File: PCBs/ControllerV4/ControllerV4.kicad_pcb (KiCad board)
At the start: 2 copper layers, 116.5 x 53 mm, 7 parts, among them J1 DB25, J2 DB25, T1 TEENSY20

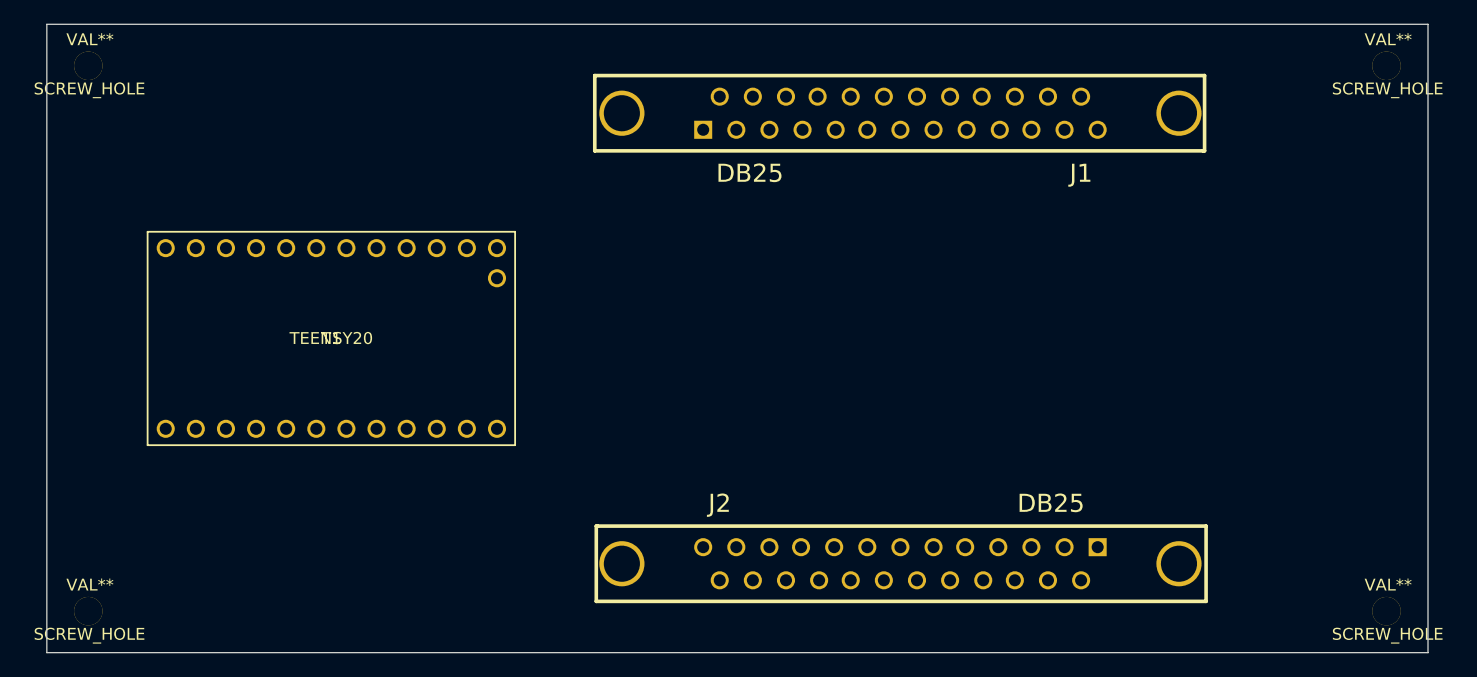
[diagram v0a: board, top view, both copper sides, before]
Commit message: Wiring controller PCB.
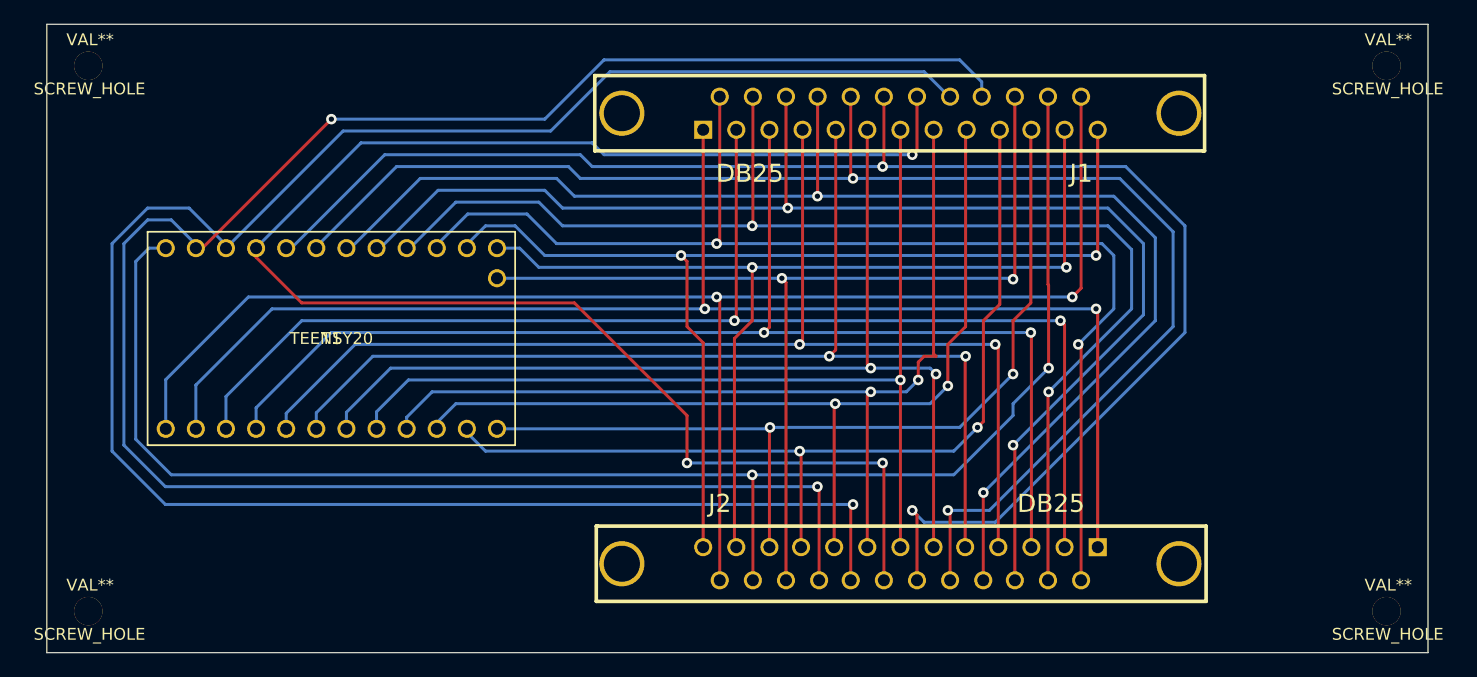
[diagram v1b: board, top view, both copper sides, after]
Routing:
- net N-000004: track 0.00 -> 168.9 mm, vias 0 -> 1
- net N-000007: track 0.00 -> 167.9 mm, vias 0 -> 2
- net N-000006: track 0.00 -> 137.6 mm, vias 0 -> 3
- net N-000005: track 0.00 -> 132.6 mm, vias 0 -> 2
- net N-000008: track 0.00 -> 132.4 mm, vias 0 -> 2
- net N-0000014: track 0.00 -> 124.7 mm, vias 0 -> 2
- net N-0000013: track 0.00 -> 123.8 mm, vias 0 -> 2
- net N-0000016: track 0.00 -> 117.6 mm, vias 0 -> 2
- net N-0000012: track 0.00 -> 116.0 mm, vias 0 -> 2
- net N-0000017: track 0.00 -> 111.2 mm, vias 0 -> 2
- net N-000009: track 0.00 -> 111.1 mm, vias 0 -> 2
- net N-0000011: track 0.00 -> 106.2 mm, vias 0 -> 2
- net N-0000018: track 0.00 -> 105.2 mm, vias 0 -> 2
- net N-0000010: track 0.00 -> 101.2 mm, vias 0 -> 2
- net N-0000019: track 0.00 -> 98.9 mm, vias 0 -> 2
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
